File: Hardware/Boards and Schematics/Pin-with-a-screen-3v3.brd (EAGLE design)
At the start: 54.5 x 35.2 mm, 44 parts, among them J1 AVR_SPI_PRG_6NS, Q2 BL8530, U1 ATMEGA328P, U2 MICRO-SD-SOCKET-SMD1:1, Y1 8MHz

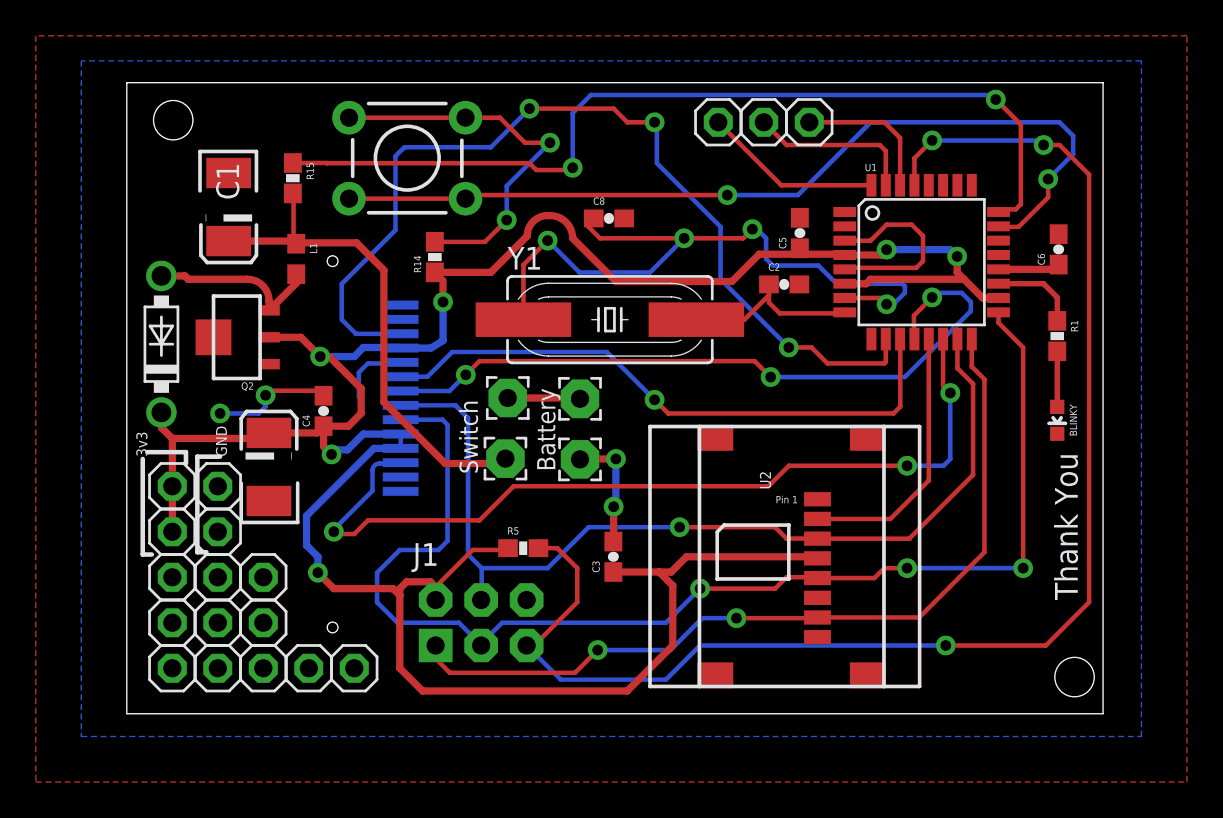
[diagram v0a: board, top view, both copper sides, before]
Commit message: Changed button to horizontal type, added screw-hole
Push button changed to horizontal with custom footprint. It replaced the
vertical push button. Some traces were re-routed to accomodate it.

Screw-hole added to bottom left of board since top left one could have
issues with push button.
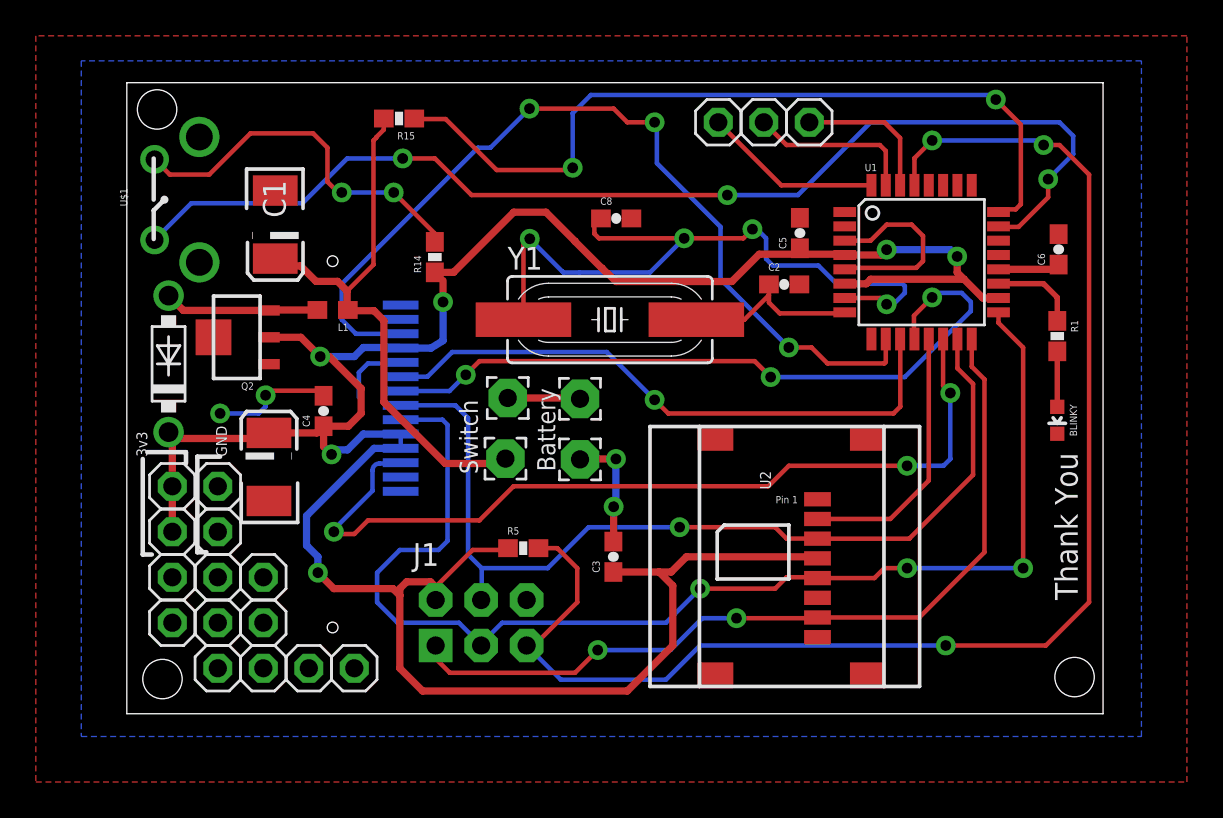
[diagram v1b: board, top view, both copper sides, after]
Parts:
- removed JP15: (no value), pinhead:1X01
- removed S1: Button McButtonface, SparkFun-Electromechanical:TACTILE-PTH
- added U$1: SWITCH-TACT-5MM-PTH-HORIZ, switches_adnan:5MM-PTH
- moved R15 6.80 mm to (15.2, 33.2), turned to 180 degrees
- moved L1 3.50 mm to (11.5, 22.5), turned to 180 degrees
- moved C1 2.78 mm to (8.29, 27.3)
- moved D1 1.17 mm to (2.33, 19.5)
- moved C8 0.40 mm to (27.3, 27.7)
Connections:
- net GND: now also U$1.GND, U$1.GND1
- net N$1: now also U$1.2; no longer S1.3, S1.4
- net N$2: now also U$1.1; no longer S1.1, S1.2
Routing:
- net N$1: track 50.0 -> 63.5 mm, vias 2 -> 3
- net BATT_VOLT: track 51.2 -> 45.4 mm
- net BATT_OUT: track 27.7 -> 31.4 mm
- net TFT_BACKLIGHT: track 52.6 -> 50.2 mm
- net LX: track 9.77 -> 8.66 mm
- net N$2: track 21.6 -> 20.8 mm
- net 3.3V: track 148.6 -> 147.9 mm
- net N$4: track 39.0 -> 39.6 mm

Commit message: Changed switch configuration, generated gerbers
Switch now connects directly to bottom side of PCB instead of being
wired to pads. Horizontal SPDT switch selected.

New gerbers generated with Seeed Studio CAM file.
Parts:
- removed JP17: (no value), pinhead:1X01
- removed PAD3, PAD4: (no value), wirepad:2,15/1,0
- moved JP18 2.68 mm to (12.7, 3.40)
- moved JP19 2.68 mm to (10.2, 3.40)
- moved JP14 1.68 mm to (7.62, 3.40)
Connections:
- net BATT_OUT: now also JP19.1; no longer PAD4.1
- net VCC_BATT_IN: now also JP18.1; no longer PAD3.1
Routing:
- net VCC_BATT_IN: track 4.05 -> 25.0 mm
- net BATT_OUT: track 31.4 -> 38.9 mm
- net TFTCS: track 49.2 -> 45.6 mm
- net SCK: track 69.4 -> 66.2 mm, vias 3 -> 7
- net N$6: track 78.7 -> 77.9 mm
- net 3.3V: track 147.9 -> 147.4 mm
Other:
- board text removed: "Switch"
